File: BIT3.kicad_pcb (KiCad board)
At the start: 2 copper layers, 121.3 x 109.4 mm, 47 parts, among them J1 Conn_02x04_Odd_Even, J2 Conn_01x02_Pin, Q1 2SC1815, SW1 SW_SPDT, SW2 SW_Push, SW3 SW_Push, U2 FODM217A, U3 FODM217A, U4 FODM217A, U5 FODM217A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

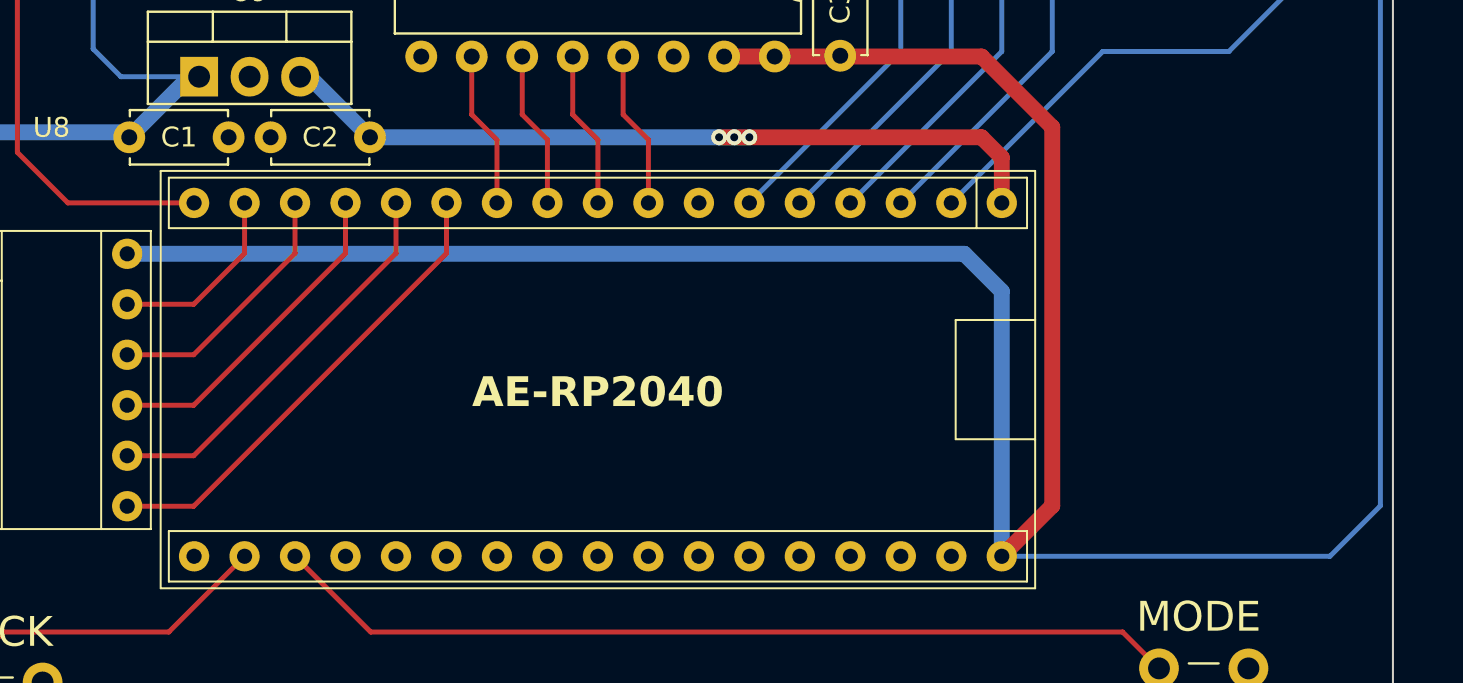
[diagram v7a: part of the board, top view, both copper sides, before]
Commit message: XBee を接続できるように変更
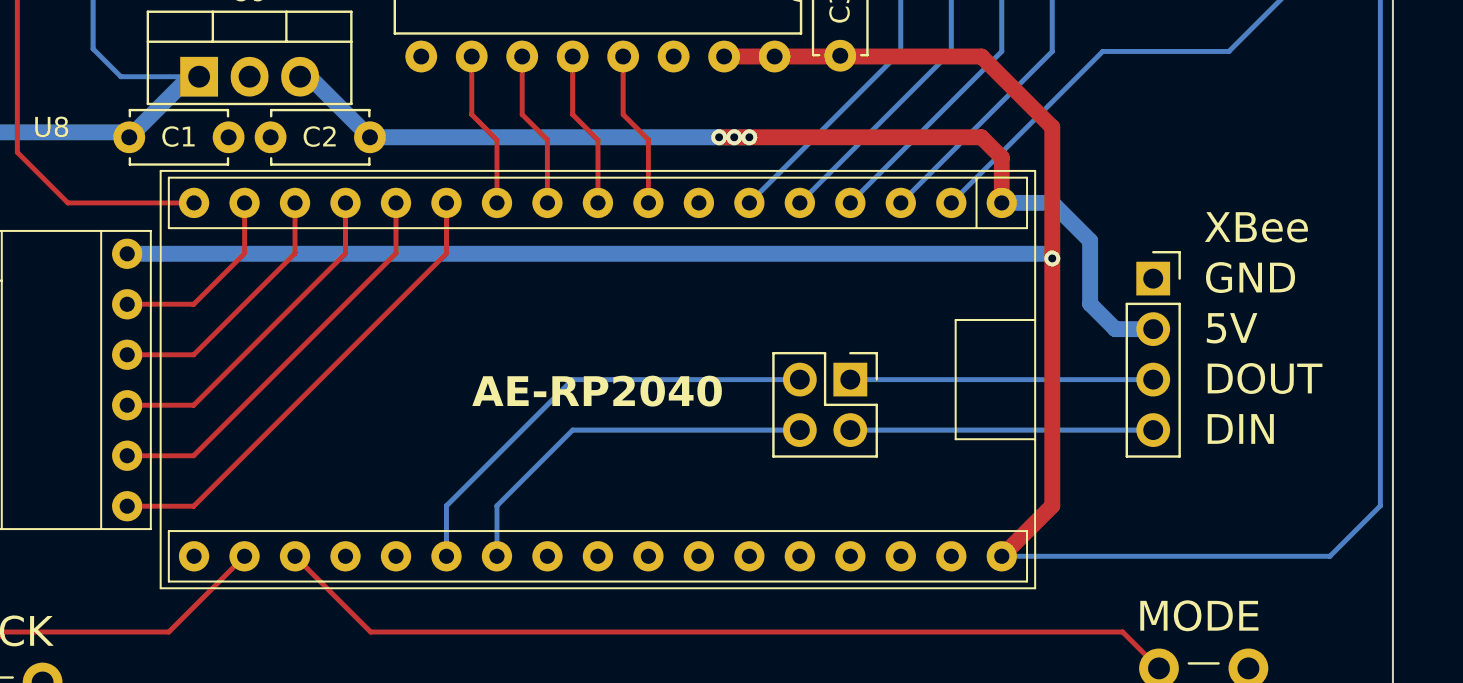
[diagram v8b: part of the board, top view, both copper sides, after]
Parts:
- added J3: Conn_01x04_Socket, Connector_PinSocket_2.54mm:PinSocket_1x04_P2.54mm_Vertical, F.Cu at (180.3, 99.1)
- added J4: Conn_02x02_Odd_Even, Connector_PinSocket_2.54mm:PinSocket_2x02_P2.54mm_Vertical, F.Cu at (165.1, 104.1)
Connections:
- U1 pad 23: unconnected-(U1-GPIO20-Pad23) -> /RasPico_RX
- U1 pad 24: unconnected-(U1-GPIO21-Pad24) -> /RasPico_TX
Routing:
- net /RasPico_RX: track 0.00 -> 23.0 mm
- net /RasPico_TX: track 0.00 -> 19.4 mm
- net /XBee_DOUT: track 0.00 -> 15.2 mm
- net /XBee_DIN: track 0.00 -> 15.2 mm
- net +5V: track 40.8 -> 52.9 mm
- net +3V3: track 287.2 -> 275.7 mm, vias 2 -> 3
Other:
- board text added: "5V"
- board text added: "DIN"
- board text added: "DOUT"
- board text added: "XBee"
